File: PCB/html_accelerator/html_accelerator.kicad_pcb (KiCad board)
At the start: 4 copper layers, 129.3 x 104.4 mm, 170 parts, among them J1 Bus_PCI_Express_x16, J2 PCIexpress_bracket, U1 MCS9990, U10 AU6438BS, U11 EMMC_4G, U12 MCS9990, U2 AP1513, U3 CAT24C256YI-GT3, U4 AU6438BS, U5 EMMC_4G, U6 EMMC_4G, U7 EMMC_4G, U8 AU6438BS, U9 AU6438BS, Y1 12MHz, Y2 12MHz, Y3 12MHz, Y4 12MHz, Y5 12MHz

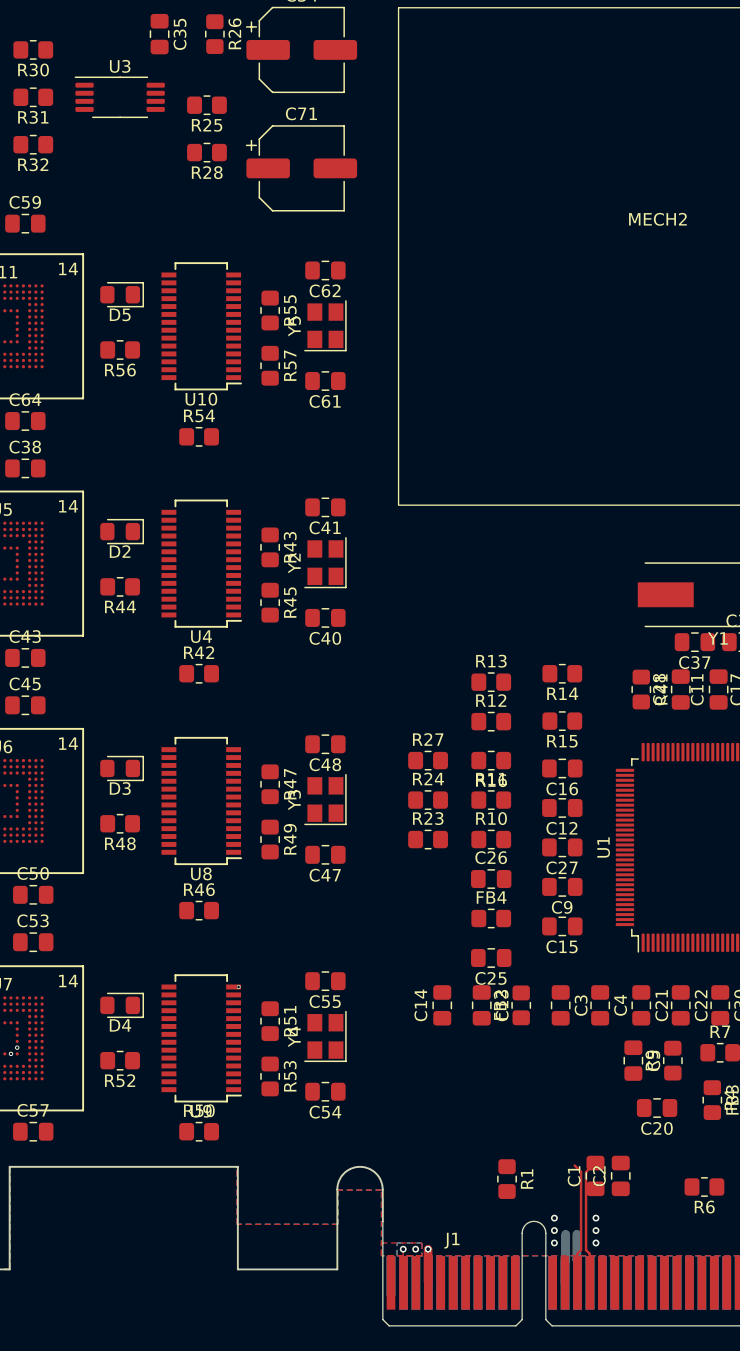
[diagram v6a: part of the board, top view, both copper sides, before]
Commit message: constraints for impedance control
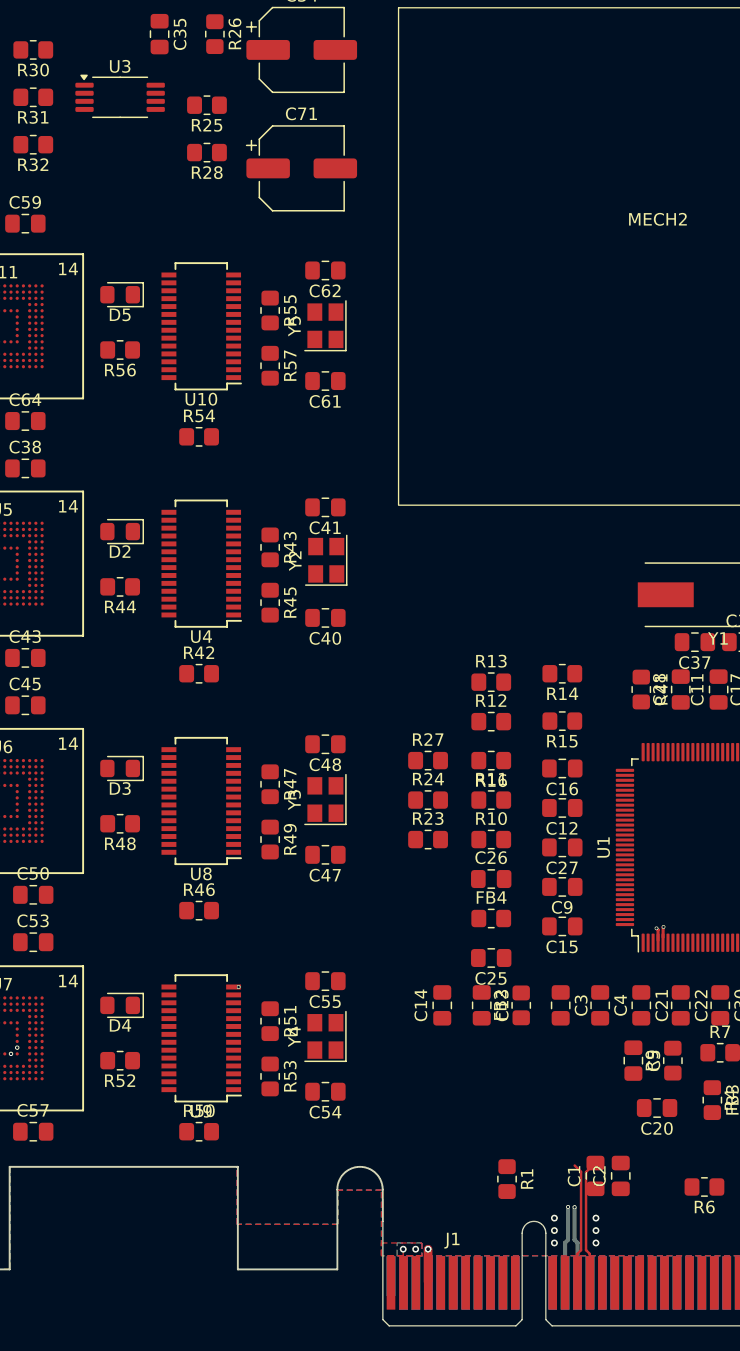
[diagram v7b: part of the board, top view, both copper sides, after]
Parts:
- moved Y2 0.20 mm to (154.8, 98.0)
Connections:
- U3 pad 5: Net-(U1E-EE_SCL) -> Net-(U1E-EE_SDA)
- U3 pad 6: Net-(U1E-EE_SDA) -> Net-(U1E-EE_SCL)
- Y2 pad 2: Net-(U4-XTAL_OUT) -> GND
- Y2 pad 3: (no net) -> Net-(U4-XTAL_OUT)
- Y2 pad 4: (no net) -> GND
- Y3 pad 2: Net-(U8-XTAL_OUT) -> GND
- Y3 pad 3: (no net) -> Net-(U8-XTAL_OUT)
- Y3 pad 4: (no net) -> GND
- Y4 pad 2: Net-(U9-XTAL_OUT) -> GND
- Y4 pad 3: (no net) -> Net-(U9-XTAL_OUT)
- Y4 pad 4: (no net) -> GND
- Y5 pad 2: Net-(U10-XTAL_OUT) -> GND
- Y5 pad 3: (no net) -> Net-(U10-XTAL_OUT)
- Y5 pad 4: (no net) -> GND
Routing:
- net /PCIE_Slot/85_PCIE_CLK_P: track 3.93 -> 34.5 mm, vias 0 -> 2
- net /PCIE_Slot/85_PCIE_CLK_N: track 3.93 -> 33.2 mm, vias 0 -> 2
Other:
- board text added: "0"
- board text added: "0 mm"
- board text added: "0.01 mm"
- board text added: "0.0152 mm"
- board text added: "0.02"
- board text added: "0.035 mm"
- board text added: "0.1000 mm / 0.2000 mm"
- board text added: "0.2000 mm"
- board text added: "0.2104 mm"
- board text added: "1"
- board text added: "1.065 mm"
- board text added: "1.6062 mm"
- board text added: "129.3160 mm x 108.9560 mm"
- board text added: "3.3"
- board text added: "4"
- board text added: "4.5"
- board text added: "B.Cu"
- board text added: "B.Mask"
- board text added: "B.Paste"
- board text added: "B.Silkscreen"
- board text added: "BOARD CHARACTERISTICS"
- board text added: "Blue"
- board text added: "Board Thickness:"
- board text added: "Board overall dimensions:"
- board text added: "Bottom Silk Screen"
- board text added: "Bottom Solder Mask"
- board text added: "Bottom Solder Paste"
- board text added: "Castellated pads:"
- board text added: "Color"
- board text added: "Copper Finish:"
- board text added: "Copper Layer Count:"
- board text added: "Dielectric 1"
- board text added: "Dielectric 2"
- board text added: "Dielectric 3"
- board text added: "ENIG"
- board text added: "Edge card connectors:"
- board text added: "Epsilon R"
- board text added: "F.Cu"
- board text added: "F.Mask"
- board text added: "F.Paste"
- board text added: "F.Silkscreen"
- board text added: "FR4"
- board text added: "FR4 natural"
- board text added: "Impedance Control:"
- board text added: "In1.Cu"
- board text added: "In2.Cu"
- board text added: "Layer Name"
- board text added: "Loss Tangent"
- board text added: "Material"
- board text added: "Min hole diameter:"
- board text added: "Min track/spacing:"
- board text added: "No"
- board text added: "Not specified"
- board text added: "Plated Board Edge:"
- board text added: "Thickness (mm)"
- board text added: "Top Silk Screen"
- board text added: "Top Solder Mask"
- board text added: "Top Solder Paste"
- board text added: "Type"
- board text added: "White"
- board text added: "Yes"
- board text added: "Yes, Bevelled"
- board text added: "copper"
- board text added: "core"
- board text added: "prepreg"
